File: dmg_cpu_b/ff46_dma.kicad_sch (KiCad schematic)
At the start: 72 parts

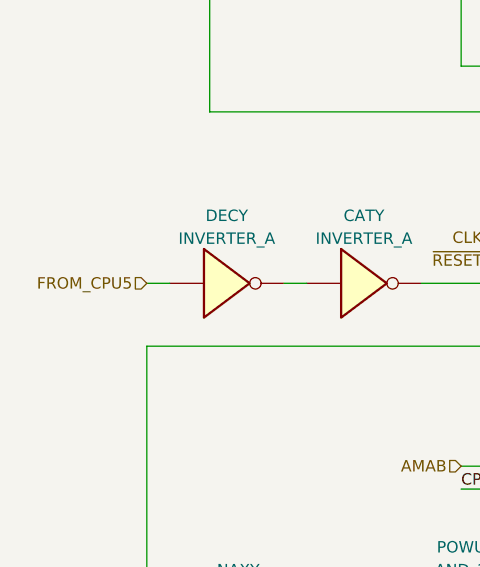
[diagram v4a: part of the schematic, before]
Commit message: VRAM interface sheet added but various edits in existing sheets. Notable merge of RESET, CLOCKS and FF04 DIV sheets
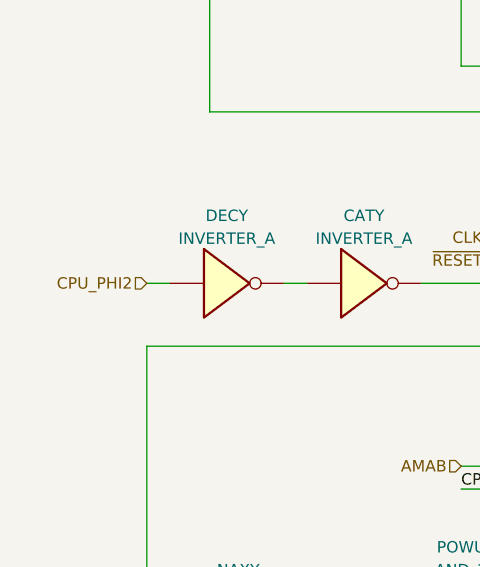
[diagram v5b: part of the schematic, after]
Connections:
- net FROM_CPU5 renamed CPU_PHI2
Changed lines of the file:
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@@
   (title_block
     (title "DMG CPU B")
-    (date "2022-03-12")
+    (date "2022-05-02")
     (rev "0")
     (company "CC-BY-SA-4.0 Régis Galland & Michael Singer -- Derived work from Furrtek")
@@
     (effects (font (size 1.27 1.27)) (justify left))
   )
-  (hierarchical_label "FROM_CPU5" (shape input) (at 35.56 98.425 180)
+  (hierarchical_label "CPU_PHI2" (shape input) (at 35.56 98.425 180)
     (effects (font (size 1.27 1.27)) (justify right))
   )

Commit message: Minor tweaks to help with clarity.
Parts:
- removed CATY, DECY: INVERTER_A, symbol DMG_CPU_Cells:INVERTER_A
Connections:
- net CPU_WR2 is gone; now on net PPU_WR: WYJA.2
- net OAM_PHI: now reaches MAKA.3 (D)
- net WYJA renamed OAM_WR
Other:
- note removed: "CPU_RD2 and CPU_WR2 only conencted to PPU registers"
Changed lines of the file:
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@@
     (stroke (width 0) (type default) (color 0 0 0 0))
   )
-  (wire (pts (xy 66.04 98.425) (xy 85.725 98.425))
+  (wire (pts (xy 75.565 98.425) (xy 85.725 98.425))
     (stroke (width 0) (type default) (color 0 0 0 0))
   )
@@
     (stroke (width 0) (type default) (color 0 0 0 0))
   )
-  (wire (pts (xy 35.56 98.425) (xy 38.1 98.425))
-    (stroke (width 0) (type default) (color 0 0 0 0))
-  )
   (wire (pts (xy 281.305 210.185) (xy 281.305 226.06))
     (stroke (width 0) (type default) (color 0 0 0 0))
@@
     (stroke (width 0) (type default) (color 0 0 0 0))
   )
-  (wire (pts (xy 50.8 98.425) (xy 53.34 98.425))
-    (stroke (width 0) (type default) (color 0 0 0 0))
-  )
   (wire (pts (xy 98.425 79.375) (xy 98.425 74.295))
     (stroke (width 0) (type default) (color 0 0 0 0))
@@
     (stroke (width 0) (type default) (color 0 0 0 0))
   )
-  (text "CPU_RD2 and CPU_WR2 only conencted to PPU registers"
-    (at 52.07 29.21 0)
-    (effects (font (size 1.27 1.27)) (justify left bottom))
-  )
   (text "8000-9FFF detect" (at 130.175 281.305 0)
     (effects (font (size 1.27 1.27)) (justify left bottom))
   )
+  (text "FF46 DMA" (at 91.44 30.48 0)
+    (effects (font (size 5 5) (thickness 1) bold) (justify left bottom))
+  )
   (text "9F detect" (at 229.87 224.79 0)
     (effects (font (size 1.27 1.27)) (justify left bottom))
   )
-  (text "FF46 DMA" (at 114.3 29.845 0)
-    (effects (font (size 1.27 1.27)) (justify left bottom))
-  )
   (label "~{DMA_PHI}" (at 267.97 210.185 0)
     (effects (font (size 1.27 1.27)) (justify left bottom))
@@
     (effects (font (size 1.27 1.27)) (justify left bottom))
   )
-  (label "CPU_WR2" (at 70.485 121.285 0)
+  (label "PPU_WR" (at 70.485 121.285 0)
     (effects (font (size 1.27 1.27)) (justify left bottom))
   )
@@
     (effects (font (size 1.27 1.27)) (justify left))
   )
-  (hierarchical_label "CPU_PHI2" (shape input) (at 35.56 98.425 180)
-    (effects (font (size 1.27 1.27)) (justify right))
-  )
   (hierarchical_label "D[0..8]" (shape bidirectional) (at 123.19 192.405 180)
     (effects (font (size 1.27 1.27)) (justify right))
@@
     (effects (font (size 1.27 1.27)) (justify right))
   )
+  (hierarchical_label "OAM_PHI" (shape input) (at 75.565 98.425 180)
+    (effects (font (size 1.27 1.27)) (justify right))
+  )
   (hierarchical_label "~{RESET6}" (shape input) (at 75.565 95.885 180)
     (effects (font (size 1.27 1.27)) (justify right))
@@
     (effects (font (size 1.27 1.27)) (justify left))
   )
-  (hierarchical_label "WYJA" (shape output) (at 106.045 123.825 0)
+  (hierarchical_label "OAM_WR" (shape output) (at 106.045 123.825 0)
     (effects (font (size 1.27 1.27)) (justify left))
   )
@@
   (hierarchical_label "DMA_ADDR_EXT" (shape output) (at 210.185 243.205 0)
     (effects (font (size 1.27 1.27)) (justify left))
-  )
-  (symbol (lib_id "DMG_CPU_Cells:INVERTER_A") (at 44.45 98.425 0) (unit 1)
-    (in_bom yes) (on_board yes)
-    (property "Reference" "DECY" (id 0) (at 44.45 90.9152 0))
-    (property "Value" "INVERTER_A" (id 1) (at 44.45 93.4521 0))
-    (property "Footprint" "" (id 2) (at 41.91 98.425 0)
-      (effects (font (size 1.27 1.27)) hide)
-    )
-    (property "Datasheet" "http://iceboy.a-singer.de/doc/dmg_cells.html#inv_a" (id 3) (at 45.72 106.045 0)
-      (effects (font (size 1.27 1.27)) hide)
-    )
-    (pin "1")
-    (pin "2")
   )
   (symbol (lib_id "DMG_CPU_Cells:NOR_2") (at 45.72 137.795 0) (unit 1)
@@
       (effects (font (size 1.27 1.27)) hide)
     )
-    (pin "1")
-    (pin "2")
-  )
-  (symbol (lib_id "DMG_CPU_Cells:INVERTER_A") (at 59.69 98.425 0) (unit 1)
-    (in_bom yes) (on_board yes)
-    (property "Reference" "CATY" (id 0) (at 59.69 90.9152 0))
-    (property "Value" "INVERTER_A" (id 1) (at 59.69 93.4521 0))
-    (property "Footprint" "" (id 2) (at 57.15 98.425 0)
-      (effects (font (size 1.27 1.27)) hide)
-    )
-    (property "Datasheet" "http://iceboy.a-singer.de/doc/dmg_cells.html#inv_a" (id 3) (at 60.96 106.045 0)
-      (effects (font (size 1.27 1.27)) hide)
-    )

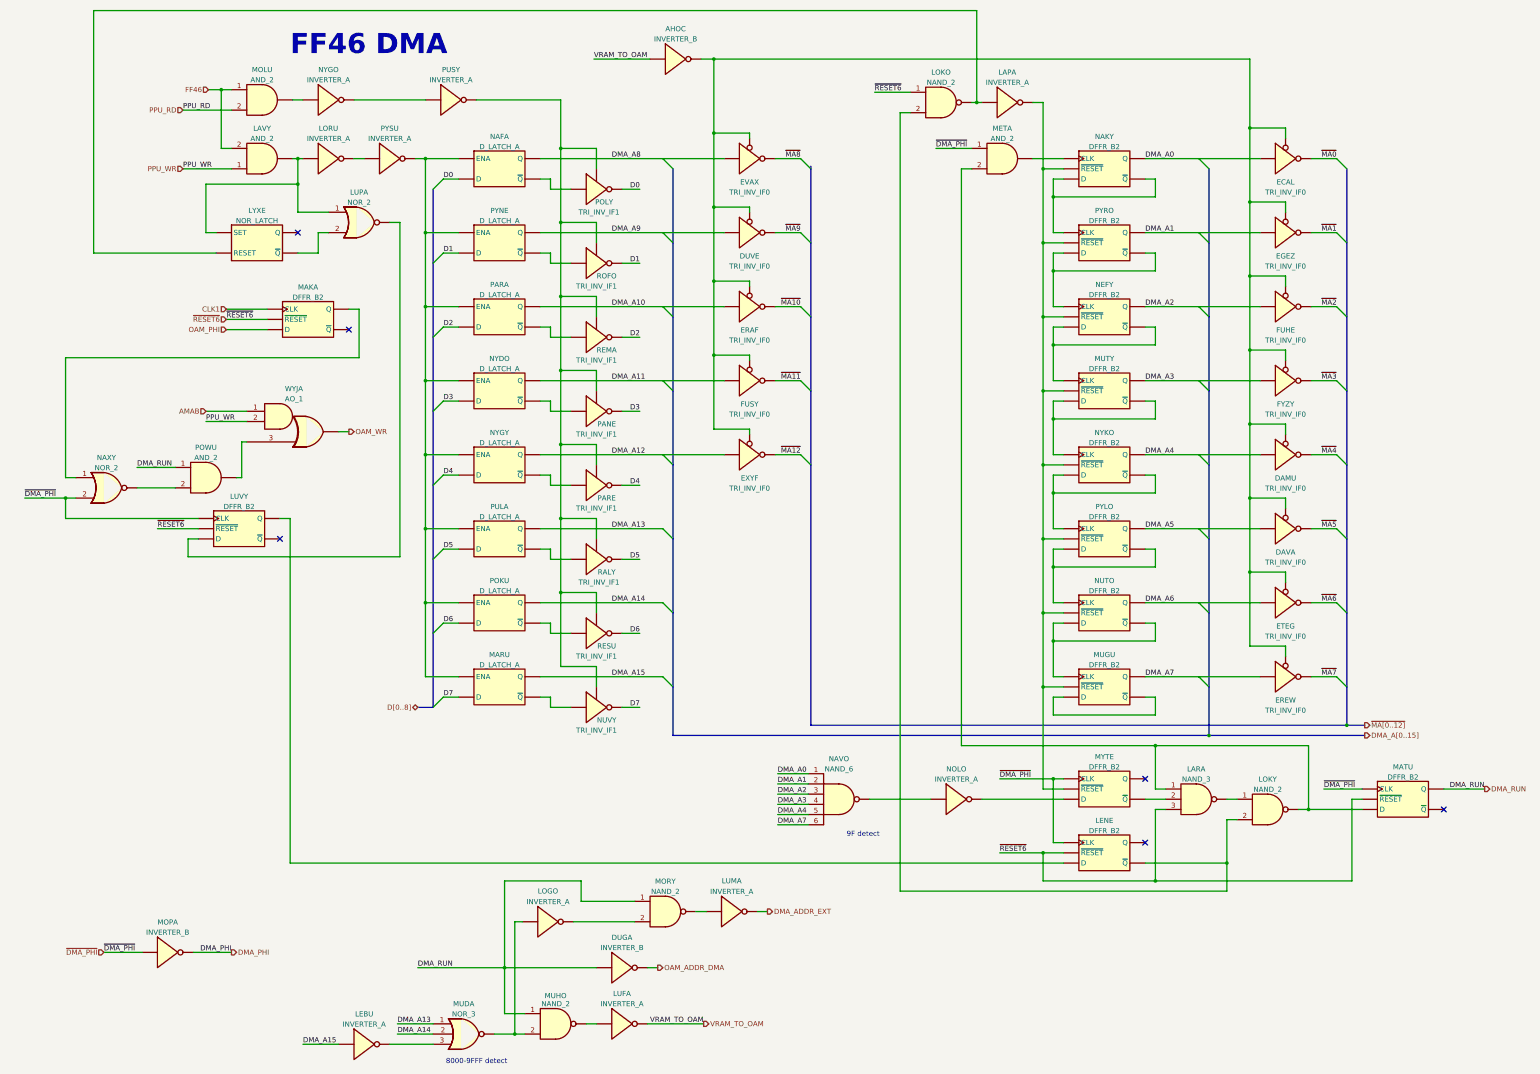
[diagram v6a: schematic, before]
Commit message: OAM and sprite x priority sheets added. OAM sheet still needs some work on it.
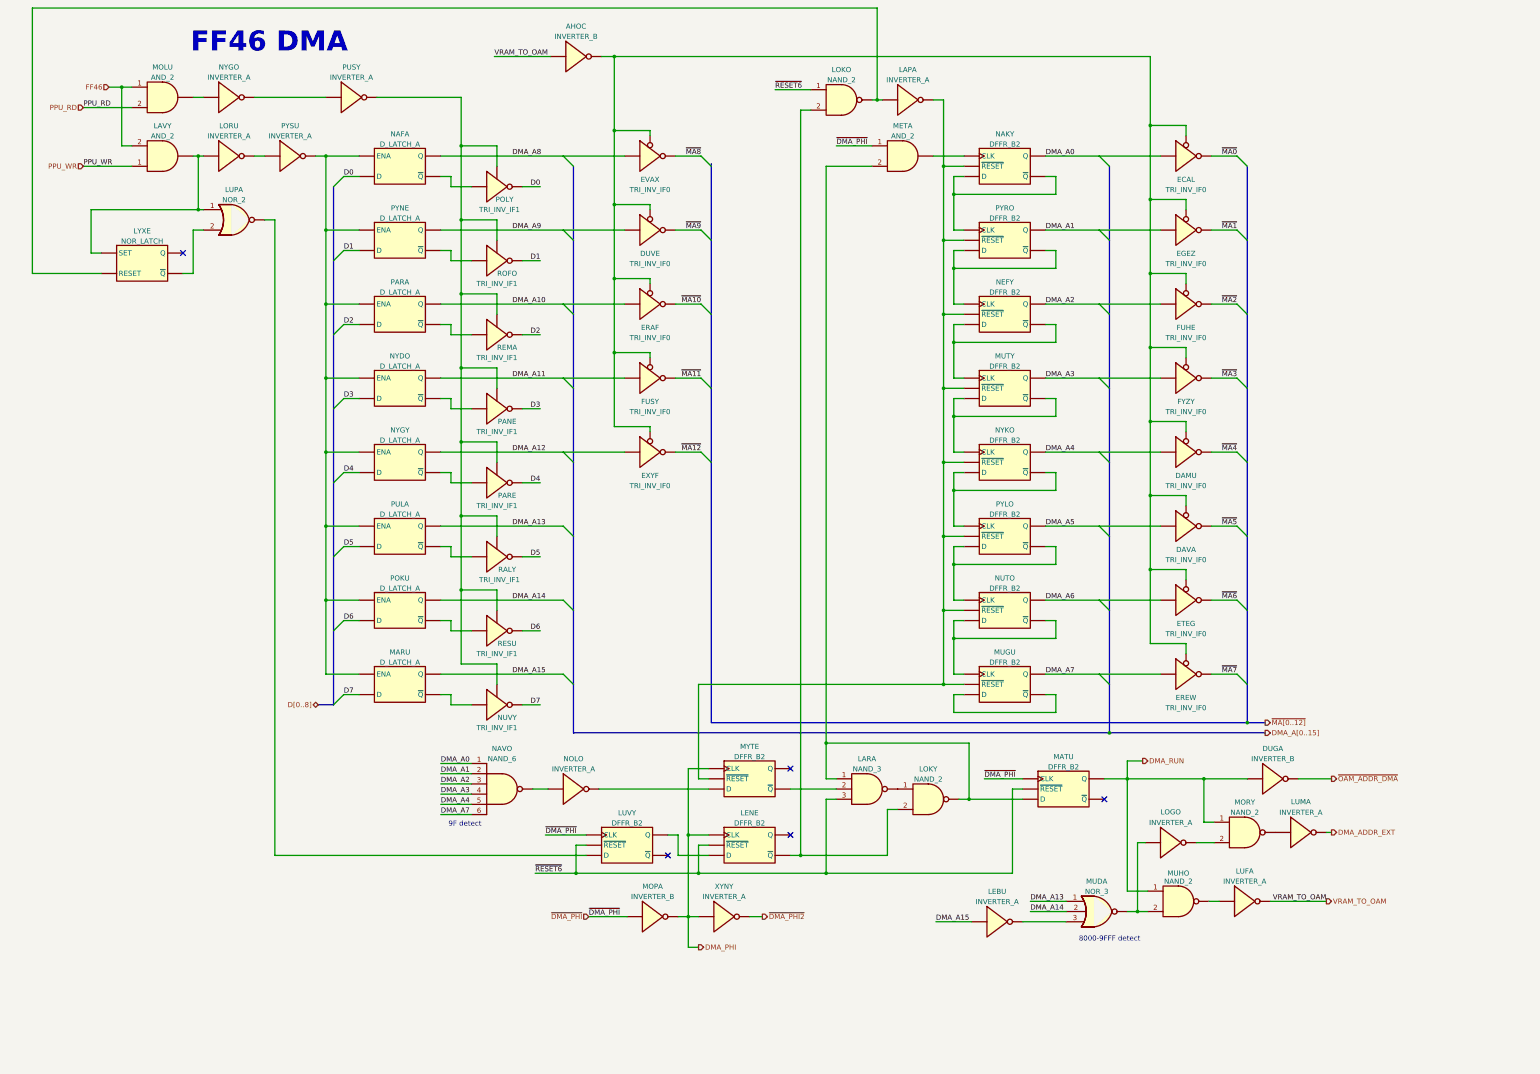
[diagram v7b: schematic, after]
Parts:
- removed MAKA: DFFR_B2, symbol DMG_CPU_Cells:DFFR_B2
- removed NAXY: NOR_2, symbol DMG_CPU_Cells:NOR_2
- removed POWU: AND_2, symbol DMG_CPU_Cells:AND_2
- removed WYJA: AO_1, symbol DMG_CPU_Cells:AO_1
- added XYNY: INVERTER_A, symbol DMG_CPU_Cells:INVERTER_A
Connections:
- net DMA_PHI: now also LENE.1 (CLK), MYTE.1 (CLK), XYNY.1
- net ~{DMA_PHI}: no longer LENE.1 (CLK), MYTE.1 (CLK)
- net OAM_ADDR_DMA renamed ~{OAM_ADDR_DMA}
- new net ~{DMA_PHI2}: XYNY.2
- no-connect marks 6 -> 5
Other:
- moved on the sheet: AHOC, DAMU, DAVA, DUGA, DUVE, ECAL, EGEZ, ERAF, EREW, ETEG, EVAX, EXYF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
